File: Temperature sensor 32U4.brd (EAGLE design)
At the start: 66 x 35.6 mm, 30 parts, among them IC1 ATMEGA32U4-AU, IC2 LM2940CS-5.0_NOPB, T1 BD139, X1 16MHz

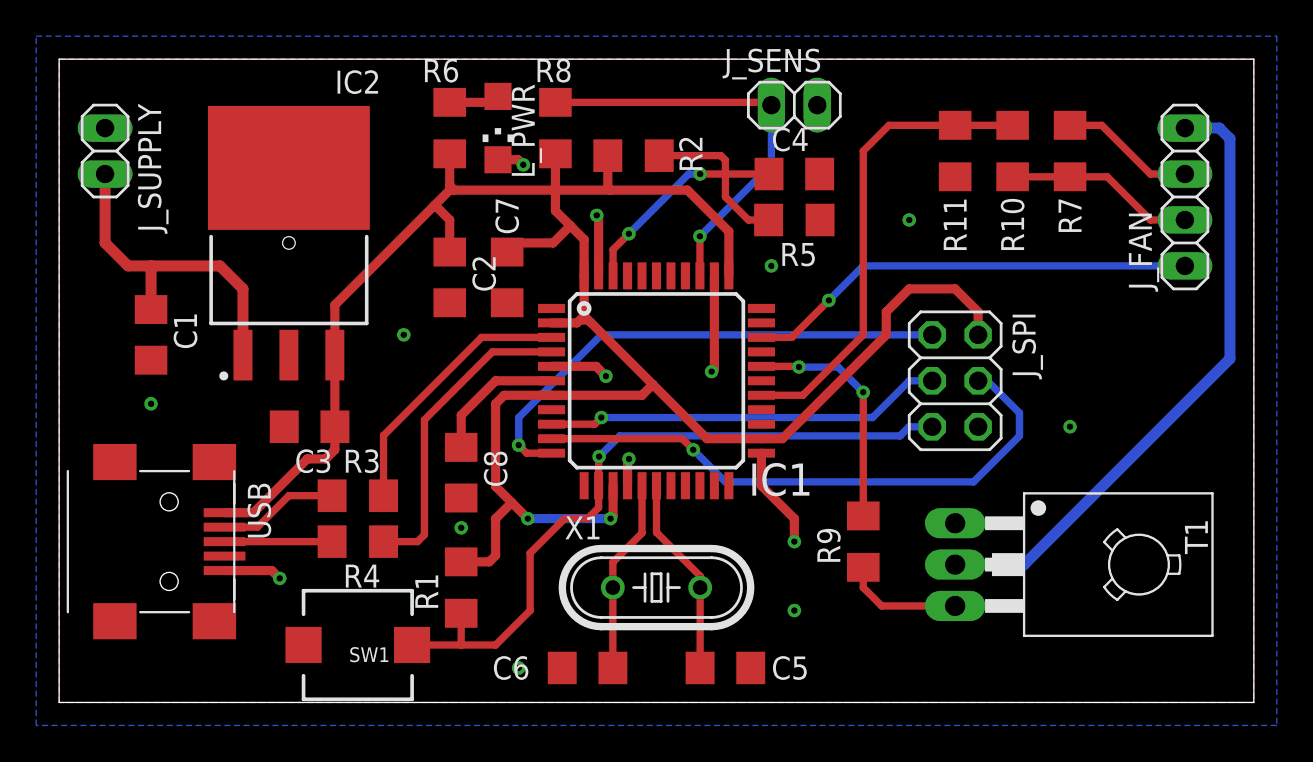
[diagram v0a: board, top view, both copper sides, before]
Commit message: Replaced BJT with a MOSFET
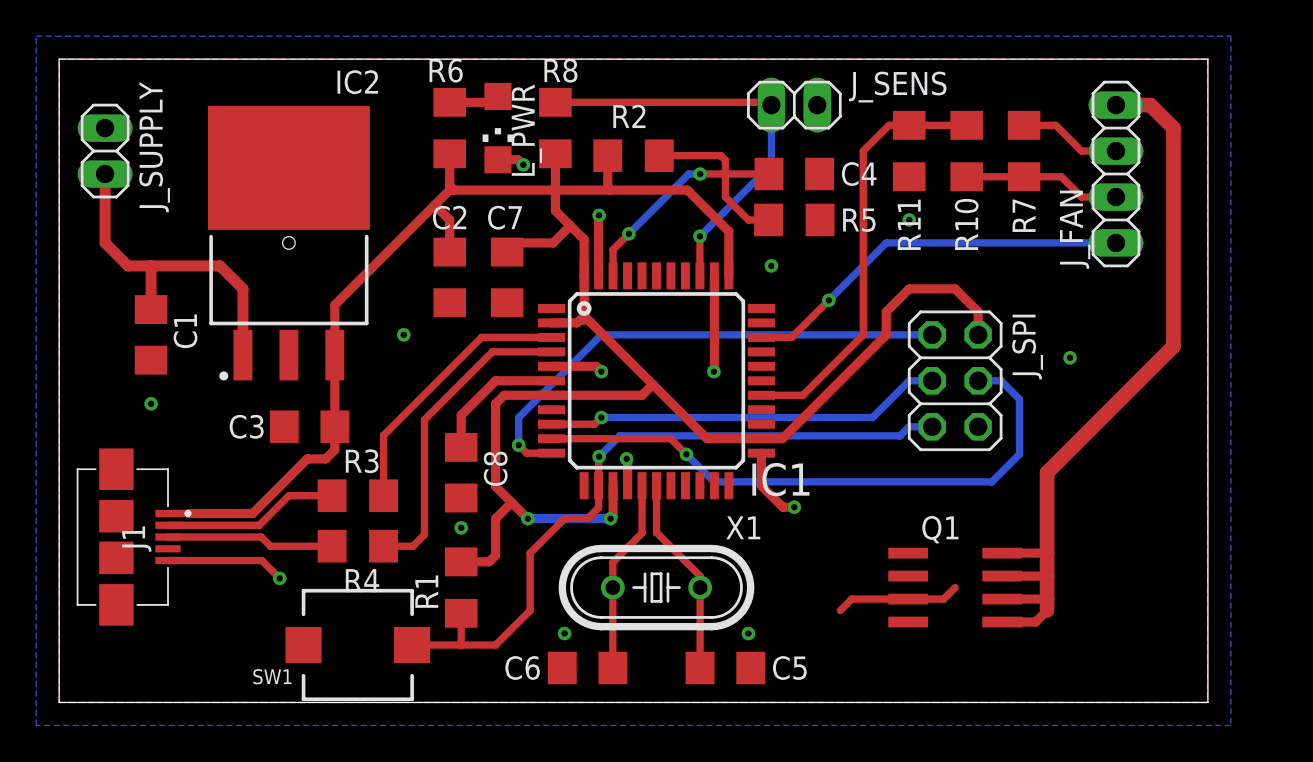
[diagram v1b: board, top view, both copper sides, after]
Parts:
- removed R9: 150, rcl:R1206
- removed T1: BD139, transistor:TO126
- removed USB: (no value), adafruit:USB-MINIB
- added J1: 10104111-0001LF, USB:101041110001LF
- added Q1: IRF7811AV, transistor-power:SO-08
- moved J_FAN 4.02 mm to (58.4, 29.2)
- moved R10 2.54 mm to (50.2, 30.5)
- moved R11 2.54 mm to (47.0, 30.5)
- moved R7 2.54 mm to (53.3, 30.5)
- moved R4 0.25 mm to (16.5, 8.64)
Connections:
- removed net FANSW: IC1.29, R9.2
- net +5V: now also J1.1; no longer USB.VBUS
- net GND: now also J1.5, J1.6, J1.7, J1.8, J1.9, Q1.1, Q1.2, Q1.3; no longer T1.1, USB.GND
- net N$2: now also IC1.29, Q1.4; no longer R9.1, T1.3
- net USB_D+: now also J1.3; no longer USB.D+
- net USB_D-: now also J1.2; no longer USB.D-
- net VOUT: now also Q1.5, Q1.6, Q1.7, Q1.8; no longer T1.2
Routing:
- net FANSW: track 13.1 -> 0.00 mm, vias 2 -> 0
- net VOUT: track 34.8 -> 43.4 mm
- net GND: track 23.9 -> 32.1 mm
- net N$2: track 6.62 -> 0.00 mm
- net USB_D+: track 5.94 -> 9.28 mm
- net PWM: track 25.0 -> 21.8 mm
- net +5V: track 125.8 -> 129.0 mm
- net USB_D-: track 6.66 -> 9.75 mm
- net TACH_IN: track 26.0 -> 23.5 mm
- net VIN: track 7.47 -> 5.67 mm
- net TACH: track 10.5 -> 8.72 mm
- net MOSI: track 32.2 -> 33.2 mm
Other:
- board size 66 x 35.6 mm -> 63.5 x 35.6 mm
